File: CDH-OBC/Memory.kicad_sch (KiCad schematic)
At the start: 22 parts, among them U2 MR25H256AMDF, U3 TPS3850H50DRCR, U4 W25N02KVZEIR, U5 PCA2129T/Q900/2_51

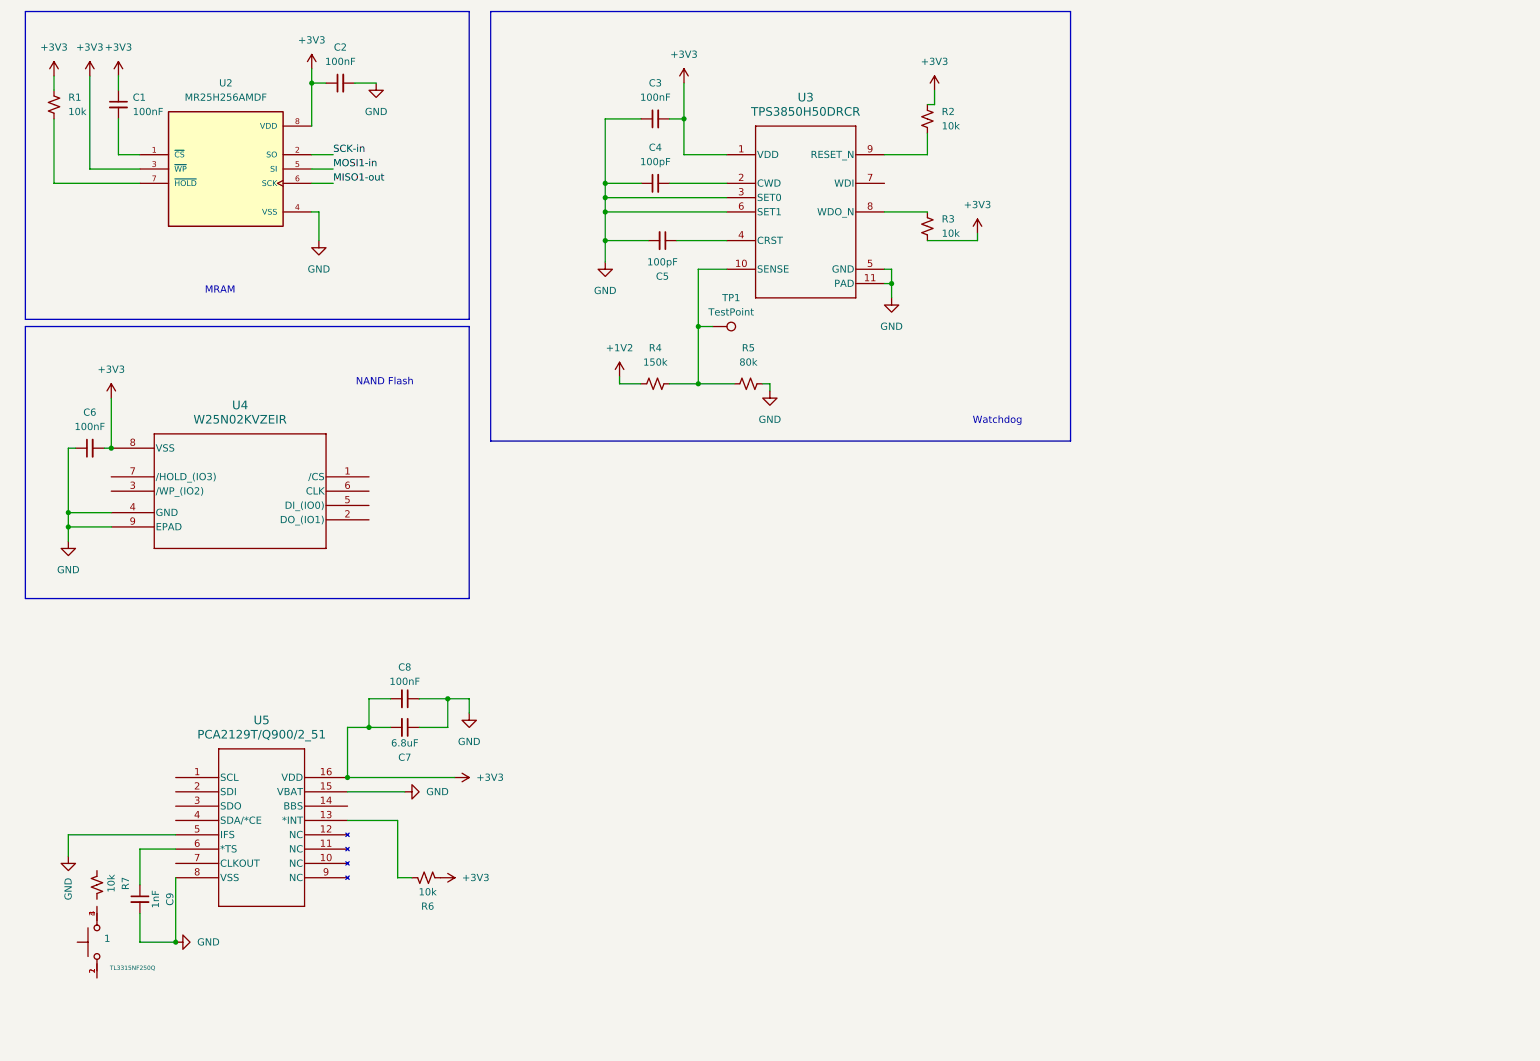
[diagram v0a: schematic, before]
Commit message: finished memory and misc subschematic
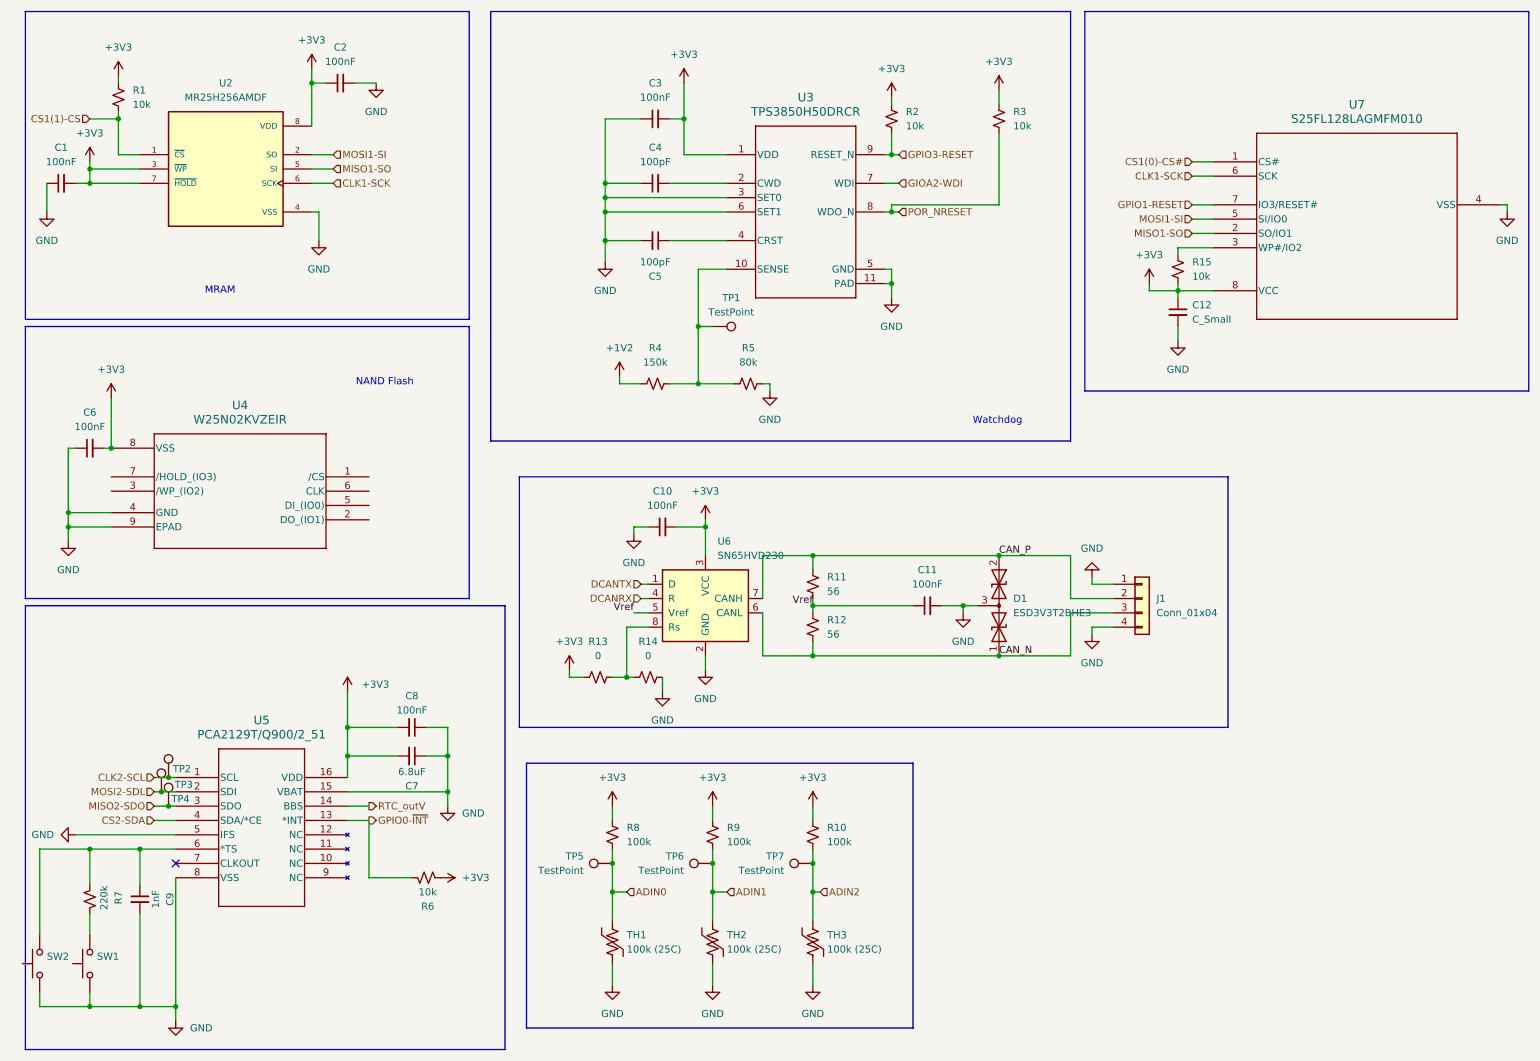
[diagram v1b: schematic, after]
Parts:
- removed 1: TL3315NF250Q, symbol OBC-lib:TL3315NF250Q
- added C10, C11: 100nF, symbol Device:C_Small
- added C12: C_Small, symbol Device:C_Small
- added D1: ESD3V3T2BHE3, symbol Device:D_TVS_Dual_AAC
- added J1: Conn_01x04, symbol Connector_Generic:Conn_01x04
- added R10, R8, R9: 100k, symbol Device:R_Small_US
- added R11, R12: 56, symbol Device:R_Small_US
- added R13, R14: 0, symbol Device:R_Small_US
- added R15: 10k, symbol Device:R_Small_US
- added SW1, SW2: SW_Push, symbol Switch:SW_Push
- added TH1, TH2, TH3: 100k (25C), symbol Device:Thermistor_US
- added TP2, TP3, TP4, TP5, TP6, TP7: TestPoint, symbol Connector:TestPoint
- added U6: SN65HVD230, Package_SO:SOIC-8_3.9x4.9mm_P1.27mm, symbol Interface_CAN_LIN:SN65HVD230
- added U7: S25FL128LAGMFM010, SOIC8_INF, symbol OBC-lib:S25FL128LAGMFM010
- R7: value 10k -> 220k
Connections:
- net +3V3: now also C1.2, U2.7 (~{HOLD}), C10.2, C12.1, R10.1, R13.1, R15.2, R8.1, R9.1, U6.3 (VCC), U7.8 (VCC); no longer C1.1
- net GND: now also C1.1, C10.1, C11.2, C12.2, D1.3 (common), J1.1 (Pin_1), J1.4 (Pin_4), R14.2, SW1.1, SW2.1, TH1.2, TH2.2, TH3.2, U6.2 (GND), U7.4 (VSS)
- net CS1(1)-CS: now reaches R1.2
- net CS1(1)-CS: now also U2.1 (~{CS}); no longer U2.7 (~{HOLD})
- net GPIO0-~{INT}: now reaches R6.1, U5.13 (*INT)
- net at C9.1, U5.6 (*TS): now also R7.2, SW2.2
- net GIOA2-WDI: now reaches U3.7 (WDI)
- net POR_NRESET: now reaches R3.2, U3.8 (WDO_N)
- net GPIO3-RESET: now reaches R2.2, U3.9 (RESET_N)
- net CLK2-SCL: now reaches U5.1 (SCL)
- net CLK2-SCL: now also TP2.1
- net RTC_outV: now reaches U5.14 (BBS)
- net MOSI2-SDL: now reaches U5.2 (SDI)
- net MOSI2-SDL: now also TP3.1
- net MISO2-SDO: now reaches U5.3 (SDO)
- net MISO2-SDO: now also TP4.1
- net CS2-SDA: now reaches U5.4 (SDA/*CE)
- net at R7.1: now also SW1.2
- net MISO1-out renamed CLK1-SCK
- net CLK1-SCK: now also U7.6 (SCK)
- net MOSI1-in renamed MISO1-SO
- net MISO1-SO: now also U7.2 (SO/IO1)
- net SCK-in renamed MOSI1-SI
- net MOSI1-SI: now also U7.5 (SI/IO0)
- new net: R13.2, R14.1, U6.8 (Rs)
- new net: R15.1, U7.3 (WP#/IO2)
- new net ADIN0: R8.2, TH1.1, TP5.1
- new net ADIN1: R9.2, TH2.1, TP6.1
- new net ADIN2: R10.2, TH3.1, TP7.1
- new net CAN_N: D1.1 (A1), J1.3 (Pin_3), R12.2, U6.6 (CANL)
- new net CAN_P: D1.2 (A2), J1.2 (Pin_2), R11.1, U6.7 (CANH)
- new net CS1(0)-CS#: U7.1 (CS#)
- new net DCANRX: U6.4 (R)
- new net DCANTX: U6.1 (D)
- new net GPIO1-RESET: U7.7 (IO3/RESET#)
- new net Vref: C11.1, R11.2, R12.1, U6.5 (Vref)
- no-connect marks 0 -> 1
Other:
- moved on the sheet: C1, C5, C7, C8, R1, R2, R3, R7

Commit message: finished bulk of the schematic
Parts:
- removed R10, R8, R9: 100k, symbol Device:R_Small_US
- removed TH1, TH2, TH3: 100k (25C), symbol Device:Thermistor_US
- removed TP5, TP6, TP7: TestPoint, symbol Connector:TestPoint
- removed U6: SN65HVD230, Package_SO:SOIC-8_3.9x4.9mm_P1.27mm, symbol Interface_CAN_LIN:SN65HVD230
- added C20, C21: 100nF, symbol Device:C_Small
- added D6: ESD3V3T2BHE3, symbol Device:D_TVS_Dual_AAC
- added J3: CAN2, symbol Connector_Generic:Conn_01x04
- added R25, R26: 0, symbol Device:R_Small_US
- added R27, R28: 56, symbol Device:R_Small_US
- added U12, U13: SN65HVD233, Package_SO:SOIC-8_3.9x4.9mm_P1.27mm, symbol Interface_CAN_LIN:SN65HVD233
- J1: value Conn_01x04 -> CAN1
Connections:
- net +3V3: now also C20.2, R25.1, U12.3 (VCC), U13.3 (VCC)
- net GND: now also C20.1, C21.2, D6.3 (common), J3.1 (Pin_1), J3.4 (Pin_4), R26.2, U12.2 (GND), U13.2 (GND)
- net at R13.2, R14.1: now also U12.8 (Rs)
- net CAN_N renamed CAN1_N
- net CAN1_N: now also U12.6 (CANL)
- net CAN_P renamed CAN1_P
- net CAN1_P: now also U12.7 (CANH)
- net Vref: no longer names the net of C11.1, R11.2, R12.1
- new net: C21.1, R27.2, R28.1
- new net: R25.2, R26.1, U13.8 (Rs)
- new net CAN2_N: D6.1 (A1), J3.3 (Pin_3), R28.2, U13.6 (CANL)
- new net CAN2_P: D6.2 (A2), J3.2 (Pin_2), R27.1, U13.7 (CANH)
- new net DCAN1RX: U12.4 (R)
- new net DCAN1TX: U12.1 (D)
- new net DCAN2RX: U13.4 (R)
- new net DCAN2TX: U13.1 (D)
- new net GIOA4-LBK: U12.5 (LBK)
- new net GIOA5-LBK: U13.5 (LBK)
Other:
- moved on the sheet: C10, C11, C3, C4, C5, D1, J1, R11, R12, R13, R14, R2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

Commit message: finished schematic
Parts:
- added R40: 10k, Resistor_SMD:R_0603_1608Metric, symbol Device:R_Small_US
- C10, C11, C20, C21: footprint (none) -> Capacitor_SMD:C_0603_1608Metric
- C12: value C_Small -> 100nF; footprint (none) -> Capacitor_SMD:C_0603_1608Metric
- D1, D6: footprint (none) -> Package_TO_SOT_SMD:SOT-23
- J1, J3: footprint (none) -> Connector_JST:JST_SH_SM04B-SRSS-TB_1x04-1MP_P1.00mm_Horizontal
- R11, R12, R13, R14, R15, R25, R26, R27, R28: footprint (none) -> Resistor_SMD:R_0603_1608Metric
- TP2, TP3, TP4: footprint (none) -> TestPoint:TestPoint_Pad_D1.0mm
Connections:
- net +3V3: now also R40.1
- net CLK1-SCK: now also U4.6 (CLK)
- net MISO1-SO: now also U4.2 (DO_(IO1))
- net MOSI1-SI: now also U4.5 (DI_(IO0))
- net CS1(2)-#CS: now reaches U4.1 (/CS)
- net at U4.3 (/WP_(IO2)): now also U4.7 (/HOLD_(IO3)), R40.2
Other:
- moved on the sheet: C6

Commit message: added some footprints
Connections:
- net CAN1_N: now also J1.2 (Pin_2); no longer J1.3 (Pin_3)
- net CAN1_P: now also J1.3 (Pin_3); no longer J1.2 (Pin_2)
- net CAN2_N: now also J3.2 (Pin_2); no longer J3.3 (Pin_3)
- net CAN2_P: now also J3.3 (Pin_3); no longer J3.2 (Pin_2)
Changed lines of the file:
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@@
 	(symbol
 		(lib_id "Connector_Generic:Conn_01x04")
-		(at 207.01 106.68 0)
+		(at 207.01 109.22 0)
+		(mirror x)
 		(unit 1)
 		(body_style 1)
@@
 		(in_pos_files yes)
 		(dnp no)
-		(fields_autoplaced yes)
 		(property "Reference" "J1"
-			(at 209.55 106.6799 0)
+			(at 209.55 109.2201 0)
 			(show_name no)
 			(do_not_autoplace no)
@@
 		)
 		(property "Value" "CAN1"
-			(at 209.55 109.2199 0)
+			(at 209.55 106.6801 0)
 			(show_name no)
 			(do_not_autoplace no)
@@
 		)
 		(property "Footprint" "Connector_JST:JST_SH_SM04B-SRSS-TB_1x04-1MP_P1.00mm_Horizontal"
-			(at 207.01 106.68 0)
+			(at 207.01 109.22 0)
 			(hide yes)
 			(show_name no)
@@
 		)
 		(property "Datasheet" ""
-			(at 207.01 106.68 0)
+			(at 207.01 109.22 0)
 			(hide yes)
 			(show_name no)
@@
 		)
 		(property "Description" "Generic connector, single row, 01x04, script generated (kicad-library-utils/schlib/autogen/connector/)"
-			(at 207.01 106.68 0)
+			(at 207.01 109.22 0)
 			(hide yes)
 			(show_name no)
@@
 	(symbol
 		(lib_id "Connector_Generic:Conn_01x04")
-		(at 213.36 152.4 0)
+		(at 213.36 154.94 0)
+		(mirror x)
 		(unit 1)
 		(body_style 1)
@@
 		(in_pos_files yes)
 		(dnp no)
-		(fields_autoplaced yes)
 		(property "Reference" "J3"
-			(at 215.9 152.3999 0)
+			(at 215.9 154.9401 0)
 			(show_name no)
 			(do_not_autoplace no)
@@
 		)
 		(property "Value" "CAN2"
-			(at 215.9 154.9399 0)
+			(at 215.9 152.4001 0)
 			(show_name no)
 			(do_not_autoplace no)
@@
 		)
 		(property "Footprint" "Connector_JST:JST_SH_SM04B-SRSS-TB_1x04-1MP_P1.00mm_Horizontal"
-			(at 213.36 152.4 0)
+			(at 213.36 154.94 0)
 			(hide yes)
 			(show_name no)
@@
 		)
 		(property "Datasheet" ""
-			(at 213.36 152.4 0)
+			(at 213.36 154.94 0)
 			(hide yes)
 			(show_name no)
@@
 		)
 		(property "Description" "Generic connector, single row, 01x04, script generated (kicad-library-utils/schlib/autogen/connector/)"
-			(at 213.36 152.4 0)
+			(at 213.36 154.94 0)
 			(hide yes)
 			(show_name no)

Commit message: finished adding footprints
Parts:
- SW1, SW2: footprint (none) -> OBC-Lib:SW_TL3315NF250Q
- U2: footprint MR25H256AMDF:SON127P500X600X90-9N -> OBC-Lib:SON127P500X600X90-9N
- U5: footprint SO16_SOT162-1_NXP -> OBC-Lib:SO16_SOT162-1_NXP
- U7: footprint SOIC8_INF -> OBC-Lib:SOIC8_INF
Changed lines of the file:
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@@
 			)
 		)
-		(property "Footprint" ""
+		(property "Footprint" "OBC-Lib:SW_TL3315NF250Q"
 			(at 21.59 184.15 0)
 			(hide yes)
@@
 			)
 		)
-		(property "Footprint" "MR25H256AMDF:SON127P500X600X90-9N"
+		(property "Footprint" "OBC-Lib:SON127P500X600X90-9N"
 			(at 50.8 43.18 0)
 			(hide yes)
@@
 			)
 		)
-		(property "Footprint" ""
+		(property "Footprint" "OBC-Lib:SW_TL3315NF250Q"
 			(at 12.7 184.15 0)
 			(hide yes)
@@
 			)
 		)
-		(property "Footprint" "SO16_SOT162-1_NXP"
+		(property "Footprint" "OBC-Lib:SO16_SOT162-1_NXP"
 			(at 38.1 147.828 0)
 			(hide yes)
@@
 			)
 		)
-		(property "Footprint" "SOIC8_INF"
+		(property "Footprint" "OBC-Lib:SOIC8_INF"
 			(at 226.06 41.91 0)
 			(hide yes)

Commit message: bulk schematic done
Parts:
- removed R1: 10k, Resistor_SMD:R_0603_1608Metric, symbol Device:R_Small_US
- removed TP2, TP3, TP4: TestPoint, TestPoint:TestPoint_Pad_D1.0mm, symbol Connector:TestPoint
- added R42, R43, R44: 10k, Resistor_SMD:R_0603_1608Metric, symbol Device:R_Small_US
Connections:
- net +3V3: now also R42.1, R43.2, R44.2; no longer U2.3 (~{WP}), U2.7 (~{HOLD})
- net MISO1-SO: now also U2.2 (SO); no longer U2.5 (SI)
- net MOSI1-SI: now also U2.5 (SI); no longer U2.2 (SO)
- net at R40.2, U4.7 (/HOLD_(IO3)): no longer U4.3 (/WP_(IO2))
- new net: R43.1, U2.3 (~{WP})
- new net: R44.1, U2.7 (~{HOLD})
- new net: R42.2, U4.3 (/WP_(IO2))
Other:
- moved on the sheet: C6
